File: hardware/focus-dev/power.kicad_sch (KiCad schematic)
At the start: 18 parts, among them J9 XT60, U11 LV14340

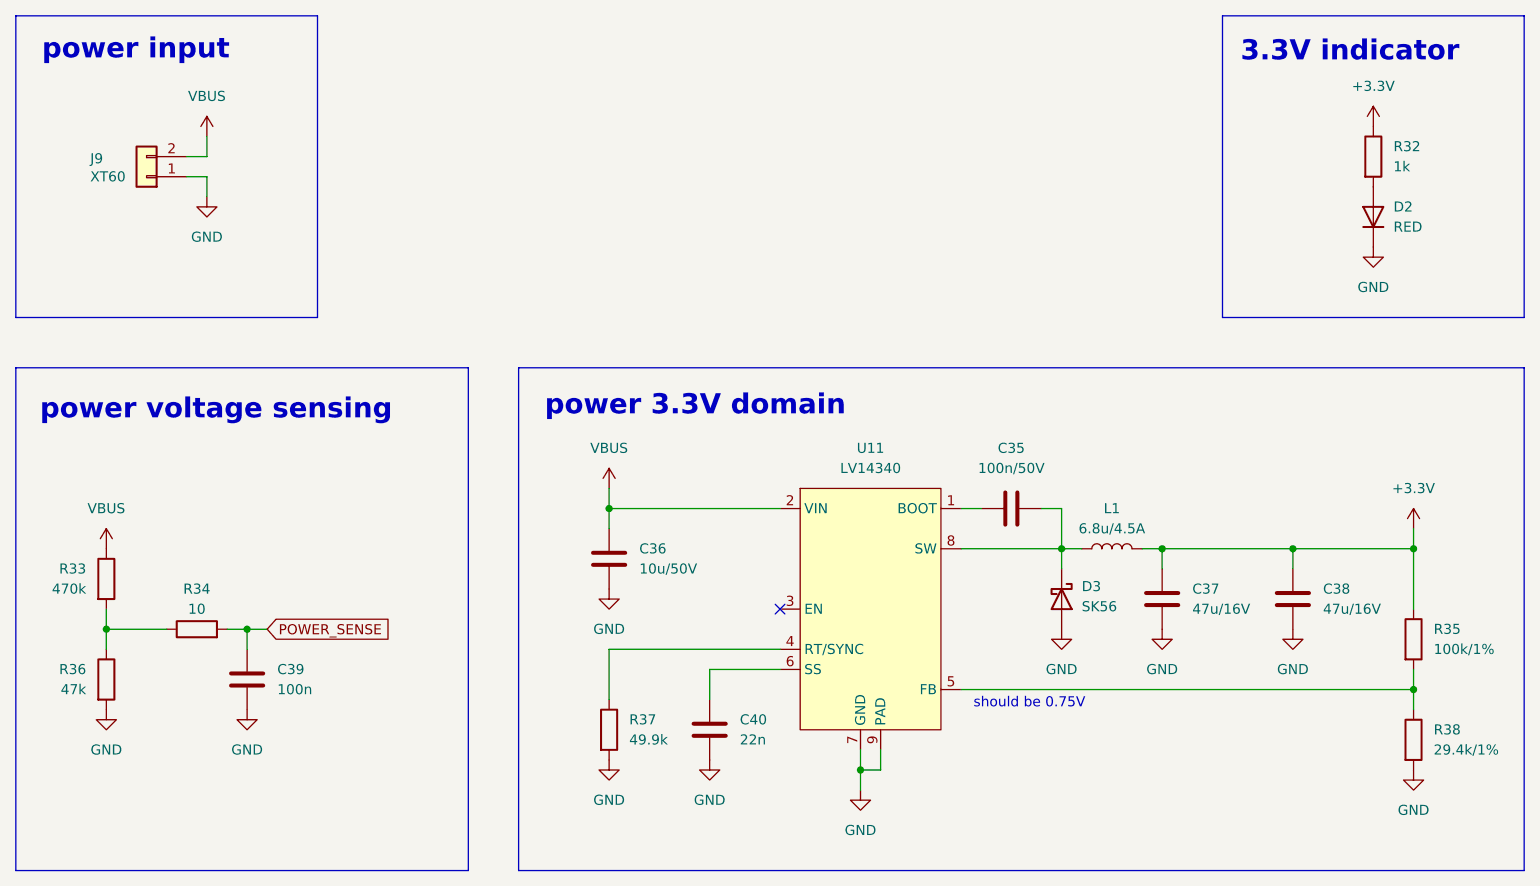
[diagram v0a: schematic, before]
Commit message: wip: remove onboard encoders
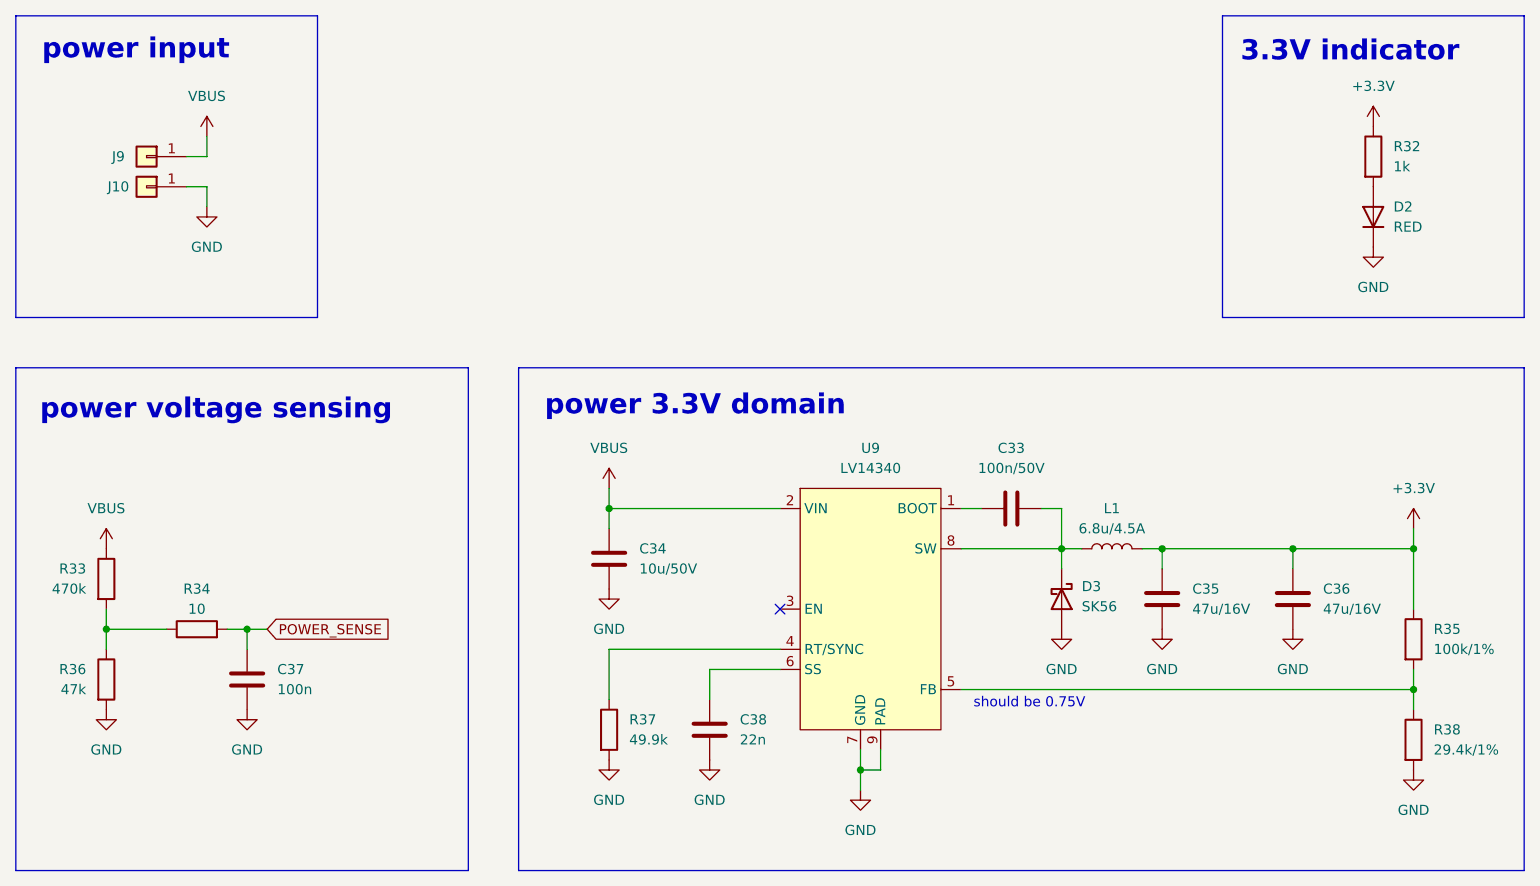
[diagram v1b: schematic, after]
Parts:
- removed J9: XT60, lib:XT60PW-M, symbol Connector_Generic:Conn_01x02
- added J10, J9: Conn_01x01, Connector_Wire:SolderWire-4sqmm_1x01_D3mm_OD6mm, symbol Connector_Generic:Conn_01x01
- renumbered C35 to C33, C36 to C34, C37 to C35, C38 to C36, C39 to C37, C40 to C38, U11 to U9
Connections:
- net GND: now also J10.1 (Pin_1)
- net VBUS: now also J9.1 (Pin_1)

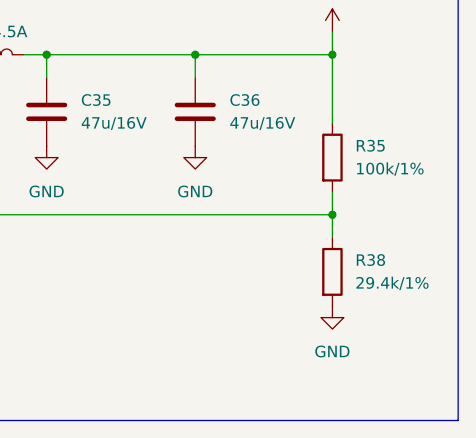
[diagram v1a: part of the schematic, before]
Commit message: wip: change resistor value
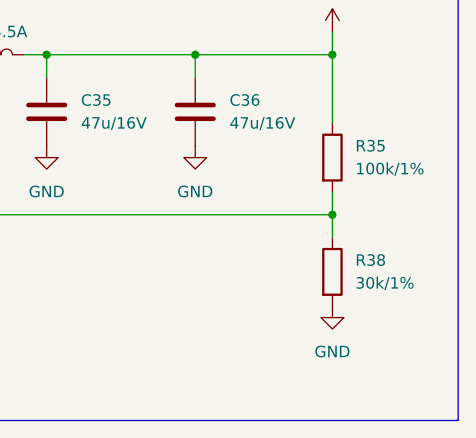
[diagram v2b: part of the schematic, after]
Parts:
- R38: value 29.4k/1% -> 30k/1%
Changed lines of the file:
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@@
 			)
 		)
-		(property "Value" "29.4k/1%"
+		(property "Value" "30k/1%"
 			(at 242.57 130.8099 0)
 			(effects
